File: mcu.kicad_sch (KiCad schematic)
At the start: 32 parts, among them J8 Conn_ARM_SWD_TagConnect_TC203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, J9 Conn_01x05_Pin, SW2 Reset, U1 nRF52840-QIAA, X1 32MHz, X2 32.768kHz

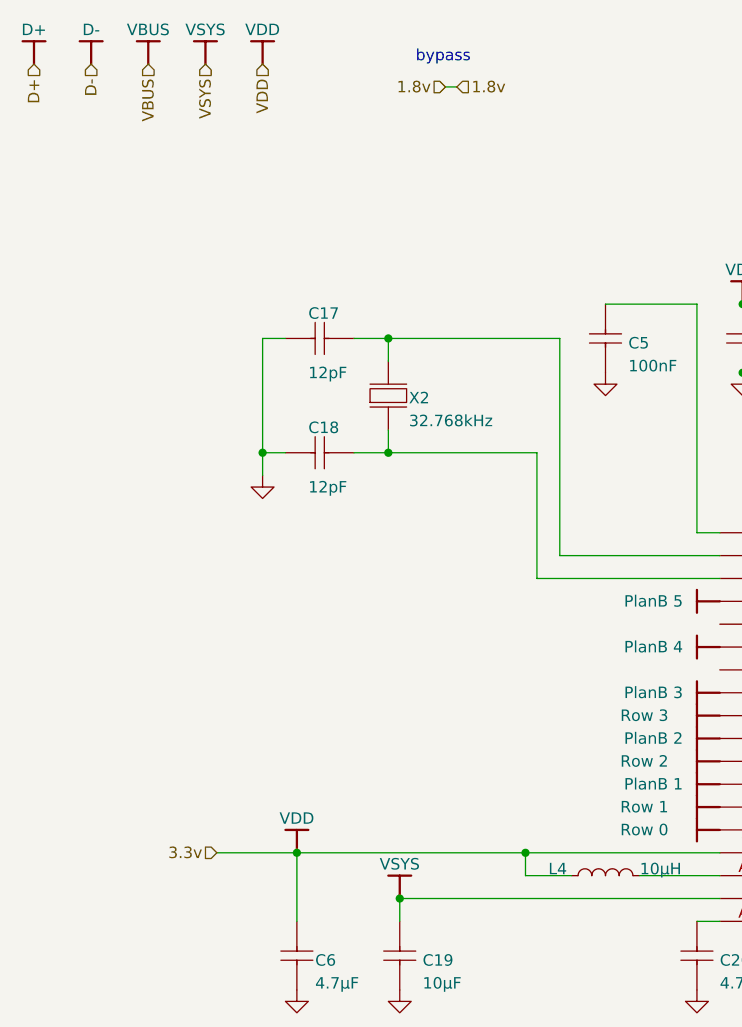
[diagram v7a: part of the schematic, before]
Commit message: Removing the 1.8v power supply option
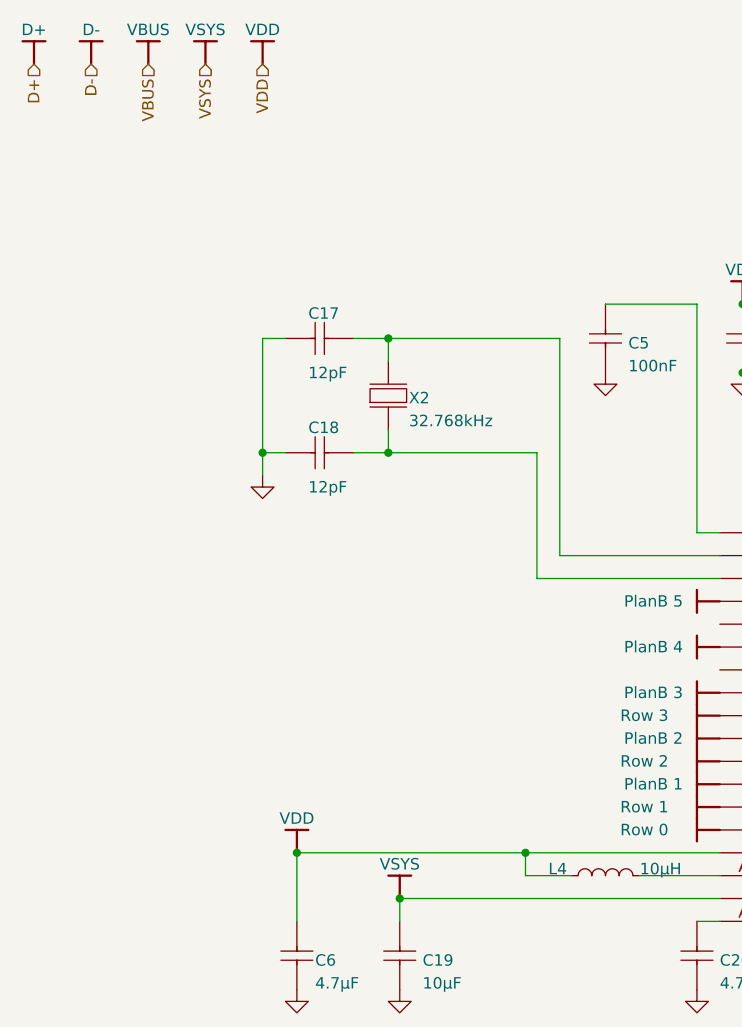
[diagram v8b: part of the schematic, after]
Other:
- note removed: "bypass"
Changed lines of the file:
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@@
 	(generator_version "9.0")
 	(paper "A4")
-	(text "bypass"
-		(exclude_from_sim no)
-		(at 68.326 25.908 0)
-		(effects
-			(font
-				(size 1.27 1.27)
-			)
-		)
-	)
 	(junction
 		(at 109.22 142.24)
@@
 	(wire
 		(pts
-			(xy 68.58 29.21) (xy 69.85 29.21)
-		)
-		(stroke
-			(width 0)
-			(type default)
-		)
-	)
-	(wire
-		(pts
 			(xy 58.42 69.85) (xy 62.23 69.85)
 		)
@@
 		(pts
 			(xy 96.52 78.74) (xy 99.06 78.74)
-		)
-		(stroke
-			(width 0)
-			(type default)
-		)
-	)
-	(wire
-		(pts
-			(xy 43.18 114.3) (xy 52.07 114.3)
 		)
 		(stroke
@@
 		)
 	)
-	(hierarchical_label "1.8v"
-		(shape input)
-		(at 69.85 29.21 0)
-		(effects
-			(font
-				(size 1.27 1.27)
-			)
-			(justify left)
-		)
-	)
 	(hierarchical_label "VSYS"
 		(shape input)
@@
 		(effects
 			(font
-				(size 1.27 1.27)
-			)
-			(justify right)
-		)
-	)
-	(hierarchical_label "3.3v"
-		(shape input)
-		(at 43.18 114.3 180)
-		(effects
-			(font
-				(size 1.27 1.27)
-			)
-			(justify right)
-		)
-	)
-	(hierarchical_label "1.8v "
-		(shape input)
-		(at 68.58 29.21 180)
-		(effects
-			(font
